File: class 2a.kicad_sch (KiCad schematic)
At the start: 36 parts, among them J1 USB_C_Receptacle, J2 Conn_01x02_Pin, J3 Conn_ARM_JTAG_SWD_10, SW1 SW_SPST, U1 STM32G030F6P6, U2 LR4054, U3 TPS613222ADBV, U4 AMS1117-3.3

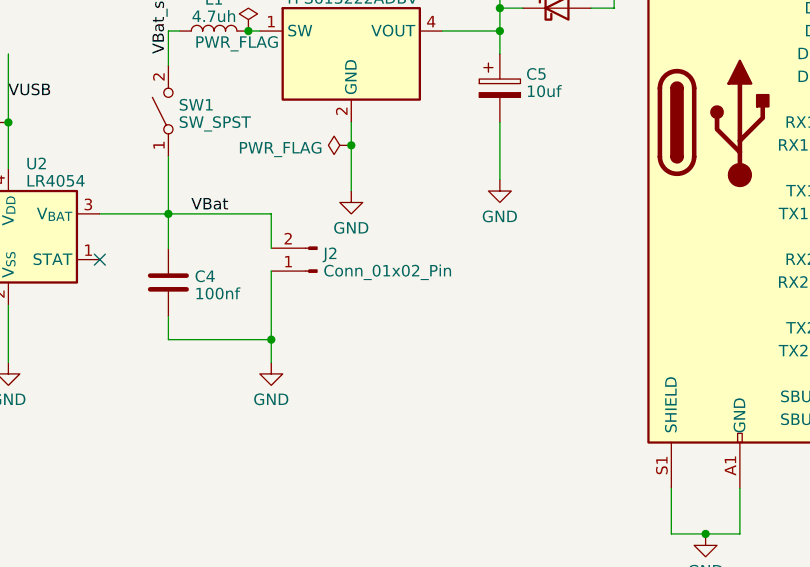
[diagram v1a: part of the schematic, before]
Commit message: rearrange things and use CR2032LIR
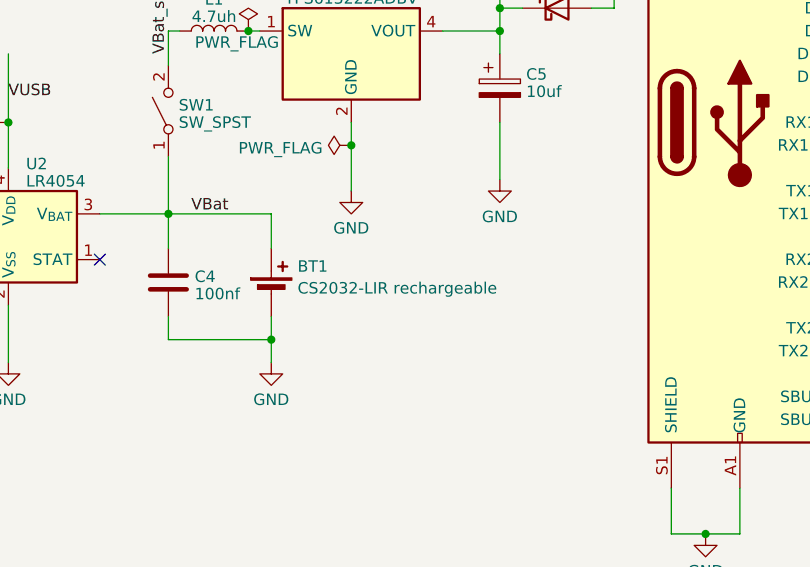
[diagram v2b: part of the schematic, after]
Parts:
- removed J2: Conn_01x02_Pin, Connector_JST:JST_PH_S2B-PH-SM4-TB_1x02-1MP_P2.00mm_Horizontal, symbol Connector:Conn_01x02_Pin
- added BT1: CS2032-LIR rechargeable, Battery:BatteryHolder_Keystone_1060_1x2032, symbol Device:Battery_Cell
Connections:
- net GND: now also BT1.2 (-)
- net VBat: now also BT1.1 (+)
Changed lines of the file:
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@@
 	)
 	(junction
-		(at 68.58 170.18)
-		(diameter 0)
-		(color 0 0 0 0)
-	)
-	(junction
 		(at 165.1 187.96)
 		(diameter 0)
@@
 	)
 	(junction
+		(at 68.58 170.18)
+		(diameter 0)
+		(color 0 0 0 0)
+	)
+	(junction
 		(at 219.71 88.9)
 		(diameter 0)
@@
 	(wire
 		(pts
-			(xy 68.58 162.56) (xy 68.58 170.18)
-		)
-		(stroke
-			(width 0)
-			(type default)
-		)
-	)
-	(wire
-		(pts
 			(xy 93.98 129.54) (xy 93.98 133.35)
 		)
@@
 	(wire
 		(pts
+			(xy 68.58 156.21) (xy 68.58 160.02)
+		)
+		(stroke
+			(width 0)
+			(type default)
+		)
+	)
+	(wire
+		(pts
 			(xy 247.65 68.58) (xy 247.65 88.9)
 		)
@@
 	(wire
 		(pts
-			(xy 68.58 156.21) (xy 68.58 160.02)
-		)
-		(stroke
-			(width 0)
-			(type default)
-		)
-	)
-	(wire
-		(pts
 			(xy 49.53 156.21) (xy 57.15 156.21)
 		)
@@
 	(wire
 		(pts
+			(xy 68.58 167.64) (xy 68.58 170.18)
+		)
+		(stroke
+			(width 0)
+			(type default)
+		)
+	)
+	(wire
+		(pts
 			(xy 113.03 191.77) (xy 116.84 191.77)
 		)
@@
 	)
 	(symbol
+		(lib_id "Device:Battery_Cell")
+		(at 68.58 165.1 0)
+		(unit 1)
+		(exclude_from_sim no)
+		(in_bom yes)
+		(on_board yes)
+		(dnp no)
+		(fields_autoplaced yes)
+		(property "Reference" "BT1"
+			(at 71.501 162.0463 0)
+			(effects
+				(font
+					(size 1.27 1.27)
+				)
+				(justify left)
+			)
+		)
+		(property "Value" "CS2032-LIR rechargeable"
+			(at 71.501 164.4706 0)
+			(effects
+				(font
+					(size 1.27 1.27)
+				)
+				(justify left)
+			)
+		)
+		(property "Footprint" "Battery:BatteryHolder_Keystone_1060_1x2032"
+			(at 68.58 163.576 90)
+			(effects
+				(font
+					(size 1.27 1.27)
+				)
+				(hide yes)
+			)
+		)
+		(property "Datasheet" "~"
+			(at 68.58 163.576 90)
+			(effects
+				(font
+					(size 1.27 1.27)
+				)
+				(hide yes)
+			)
+		)
+		(property "Description" "Single-cell battery"
+			(at 68.58 165.1 0)
+			(effects
+				(font
+					(size 1.27 1.27)
+				)
+				(hide yes)
+			)
+		)
+		(pin "1"
+		)
+		(pin "2"
+		)
+		(instances
+			(project ""
+				(path "/b0f42d21-78ce-41e8-b624-34371c0ceb55"
+					(reference "BT1")
+					(unit 1)
+				)
+			)
+		)
+	)
+	(symbol
 		(lib_id "power:GND")
 		(at 276.86 110.49 0)
@@
 					(unit 1)
 				)
-			)
-		)
-	)
-	(symbol
-		(lib_id "Connector:Conn_01x02_Pin")
-		(at 73.66 162.56 180)
-		(unit 1)
-		(exclude_from_sim no)
-		(in_bom yes)
-		(on_board yes)
-		(dnp no)
-		(fields_autoplaced yes)
-		(property "Reference" "J2"
-			(at 74.3712 160.6463 0)
-			(effects
-				(font
-					(size 1.27 1.27)
-				)
-				(justify right)
-			)
-		)
-		(property "Value" "Conn_01x02_Pin"
-			(at 74.3712 162.5673 0)
-			(effects
-				(font
-					(size 1.27 1.27)
-				)
-				(justify right)
-			)
-		)
-		(property "Footprint" "Connector_JST:JST_PH_S2B-PH-SM4-TB_1x02-1MP_P2.00mm_Horizontal"
-			(at 73.66 162.56 0)
-			(effects
-				(font
-					(size 1.27 1.27)
-				)
-				(hide yes)
-			)
-		)
-		(property "Datasheet" "~"
-			(at 73.66 162.56 0)
-			(effects
-				(font
-					(size 1.27 1.27)
-				)
-				(hide yes)
-			)
-		)
-		(property "Description" ""
-			(at 73.66 162.56 0)
-			(effects
-				(font
-					(size 1.27 1.27)
-				)
-				(hide yes)
-			)
-		)
-		(property "LCSC" "C173752"
-			(at 73.66 162.56 0)
-			(effects
-				(font
-					(size 1.27 1.27)
-				)
-				(hide yes)
-			)
-		)
-		(property "LCSC Part" "C173752"
-			(at 73.66 162.56 0)
-			(effects
-				(font
-					(size 1.27 1.27)
-				)
-				(hide yes)
-			)
-		)
-		(pin "1"
-		)
-		(pin "2"
-		)
-		(instances
-			(project "class 2a"
-				(path "/b0f42d21-78ce-41e8-b624-34371c0ceb55"
-					(reference "J2")
-					(unit 1)
-				)
